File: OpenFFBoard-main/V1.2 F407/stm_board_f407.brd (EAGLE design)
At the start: 60 x 60 mm, 60 parts, among them J1 10118193-0001LF, SW1 TL3342F160QG/TR, SW2 TL3342F160QG/TR, U1 STM32F407VGT6, U2 TJA1051T/3, U3 LM1117, X1 8MHz

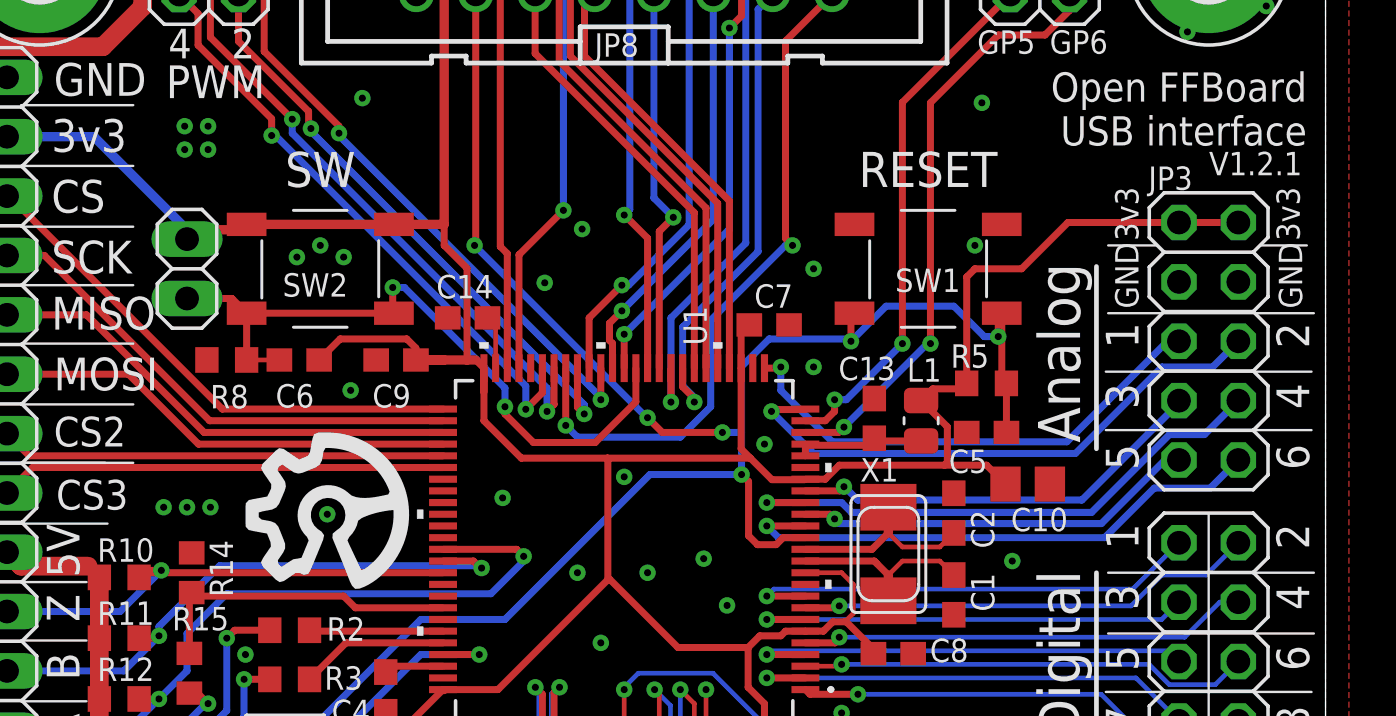
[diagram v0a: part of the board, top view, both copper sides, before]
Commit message: Swapped encoder Z pin on F407 board
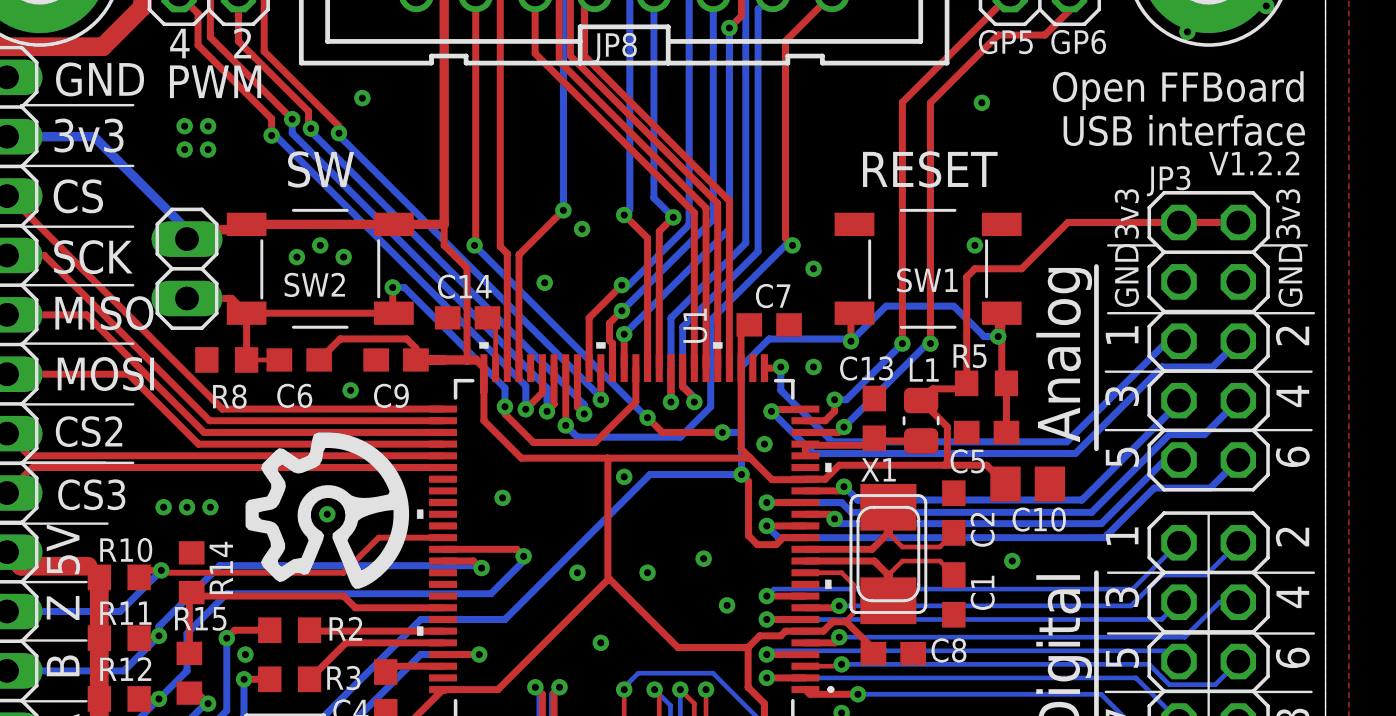
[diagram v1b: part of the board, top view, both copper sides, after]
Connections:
- net ENC_Z: now also U1.62; no longer U1.65
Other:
- board text added: "V1.2.2"
- board text removed: "JLCJLCJLCJLC"
- board text removed: "V1.2.1"
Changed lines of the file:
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@@
 <drawing>
 <settings>
-<setting alwaysvectorfont="yes"/>
+<setting alwaysvectorfont="no"/>
 <setting verticaltext="up"/>
 </settings>
@@
 <text x="59.2" y="-9.6" size="1.25" layer="21" rot="R180">Open FFBoard
 USB interface</text>
-<text x="59" y="-13" size="1" layer="21" rot="R180">V1.2.1</text>
+<text x="59" y="-13" size="1" layer="21" rot="R180">V1.2.2</text>
 <text x="21.5" y="-8.55" size="1" layer="22" font="vector" rot="MR270">GND | 5V</text>
 <text x="24" y="-8.5" size="1" layer="22" font="vector" rot="MR270">RST | 3V3</text>
@@
 <text x="53.6" y="-46.1" size="1.4" layer="21" rot="R90">CLIP</text>
 <text x="45.6" y="-46.1" size="1.4" layer="21" rot="R90">PWR</text>
-<text x="35" y="-29.5" size="0.9" layer="22" rot="MR0">JLCJLCJLCJLC</text>
 <wire x1="24.9" y1="-57" x2="24.9" y2="-60" width="0.1016" layer="21"/>
 <wire x1="22.3" y1="-57" x2="22.3" y2="-60" width="0.1016" layer="21"/>
@@
 <text x="47.4" y="-1.3" size="0.8128" layer="22" font="vector" rot="MR0">TX</text>
 <text x="49.9" y="-9.5" size="0.8128" layer="22" font="vector" rot="MR0">TIM/ADC</text>
-<text x="47.6" y="-13.3" size="1" layer="22" font="vector" rot="MR180">V1.2.1</text>
+<text x="47.6" y="-13.3" size="1" layer="22" font="vector" rot="MR180">V1.2.2</text>
 <wire x1="3" y1="-26.3" x2="7.8" y2="-26.3" width="0.1016" layer="21"/>
 <wire x1="4.2" y1="-26.3" x2="2.9" y2="-26.3" width="0.1" layer="22"/>
@@
 <contactref element="JP5" pad="2"/>
 <contactref element="R10" pad="2"/>
-<contactref element="U1" pad="65"/>
-<wire x1="22.25" y1="-31" x2="9.45" y2="-31" width="0.3" layer="1"/>
 <wire x1="9.45" y1="-31" x2="9.25" y2="-31.2" width="0.3" layer="1"/>
 <wire x1="3.6" y1="-32.66" x2="8.44" y2="-32.66" width="0.3" layer="16"/>
@@
 <wire x1="10.2" y1="-30.9" x2="9.55" y2="-30.9" width="0.3" layer="1"/>
 <wire x1="9.25" y1="-31.2" x2="9.55" y2="-30.9" width="0.3" layer="1"/>
+<contactref element="U1" pad="62"/>
+<wire x1="22.25" y1="-29.5" x2="19.5" y2="-29.5" width="0.254" layer="1"/>
+<wire x1="19.5" y1="-29.5" x2="18" y2="-31" width="0.254" layer="1"/>
+<wire x1="18" y1="-31" x2="10.3" y2="-31" width="0.254" layer="1"/>
+<wire x1="10.3" y1="-31" x2="10.2" y2="-30.9" width="0.254" layer="1"/>
 </signal>
 <signal name="I2C_SDA">
